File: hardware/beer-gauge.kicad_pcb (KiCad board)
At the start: 4 copper layers, 69.8 x 95.2 mm, 70 parts, among them J1 OLED_MODULE, P1 CONN_01X04, P2 CONN_01X04, P3 CONN_01X04, P4 CONN_01X04, P5 USB_OTG, SW1 SW_PUSH, U1 ADS1232, U2 LP38691, U3 MKL02Z32, U4 MK20DX256VLH7, U5 TCA9543A, U6 SN74LVC1G58, Y1 16 MHz, Y2 32.768 kHz

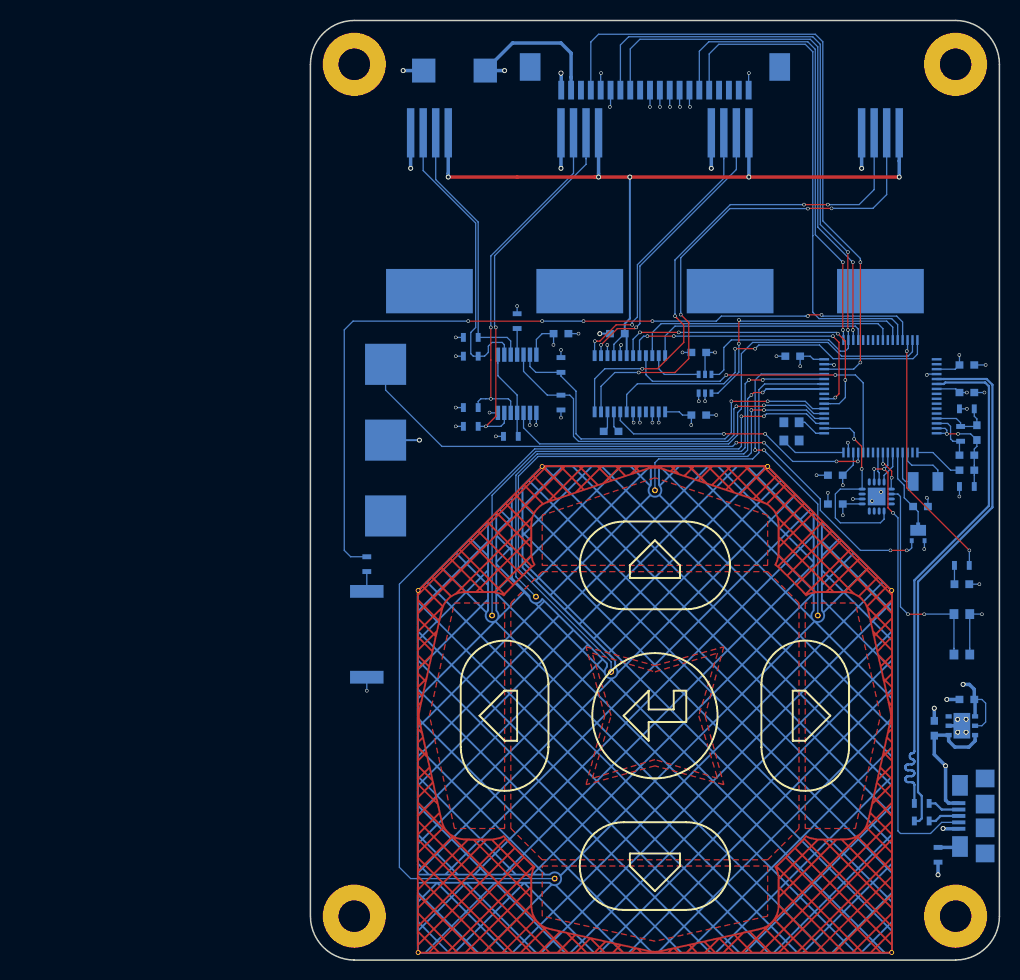
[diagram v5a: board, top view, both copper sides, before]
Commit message: Added DC jack for 5V input.  Updated layout
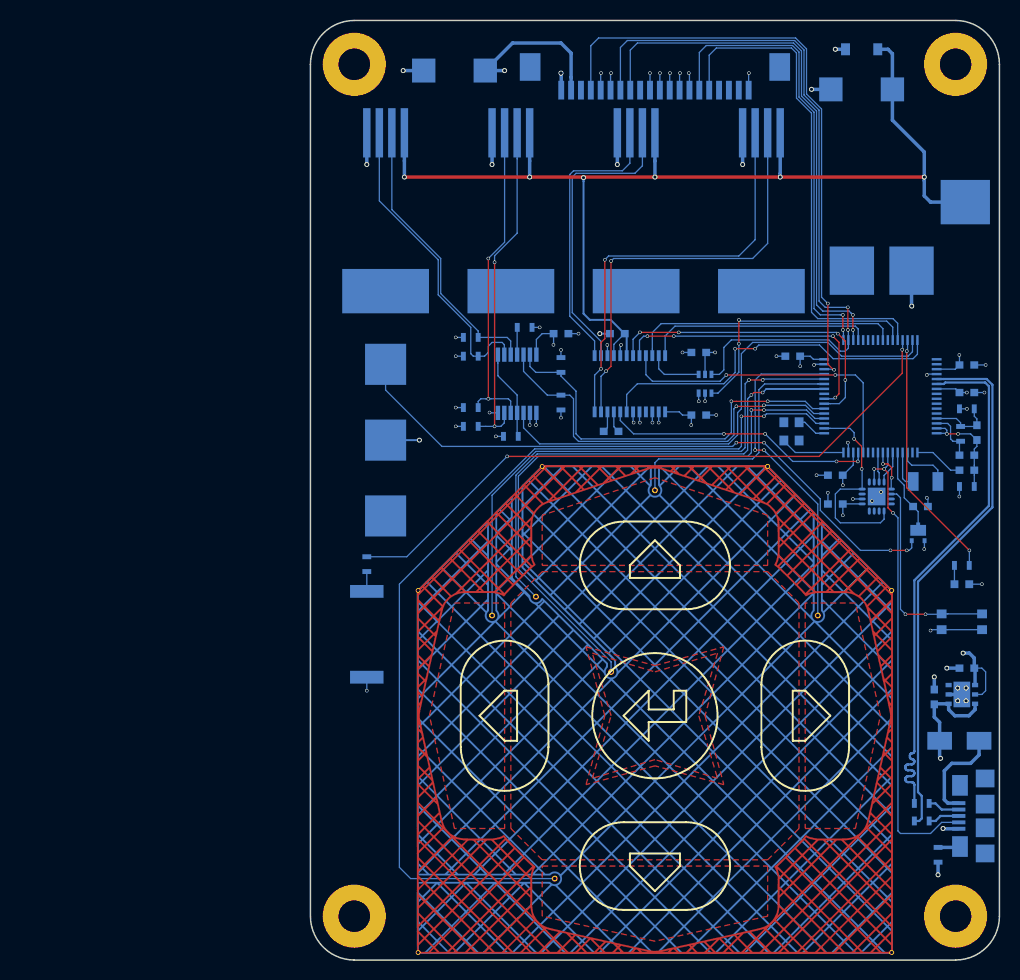
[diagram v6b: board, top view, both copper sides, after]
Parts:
- added C18: 100u, Capacitors_Tantalum_SMD:TantalC_SizeD_EIA-7343_Reflow, B.Cu at (193.0, 52.7)
- added CON1: BARREL_JACK, footprint:PJ-070AH-SMT, B.Cu at (196.8, 64.1)
- added D3: DDZ6V2B, Diodes_SMD:SOD-123, B.Cu at (193.0, 48.6)
- added D4: S1B, Diodes_SMD:SMA_Standard, B.Cu at (202.9, 118.7)
- moved P1 12.1 mm to (182.9, 64.8)
- moved P2 9.53 mm to (170.2, 64.8)
- moved P3 6.99 mm to (157.5, 64.8)
- moved P4 4.44 mm to (144.8, 64.8)
- moved C5 3.17 mm to (200.4, 114.3)
- moved C7 3.17 mm to (203.7, 111.4)
- moved U2 3.17 mm to (203.2, 114.0)
- moved SW1 1.27 mm to (203.2, 106.7), turned to 0 degrees
- moved R8 0.99 mm to (158.9, 76.8), turned to 180 degrees
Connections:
- P5 pad 1: +5V -> Net-(D4-Pad2)
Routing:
- net +5V: track 166.5 -> 192.2 mm, vias 6 -> 7
- net /Teensy/6: track 84.3 -> 65.4 mm, vias 6 -> 2
- net Net-(D4-Pad2): track 0.00 -> 10.2 mm
- net Net-(P1-Pad2): track 53.0 -> 43.5 mm, vias 4 -> 2
- net Net-(P1-Pad3): track 51.6 -> 42.8 mm, vias 4 -> 2
- net GND: track 78.8 -> 84.3 mm, vias 54 -> 57
- net /Teensy/9: track 67.1 -> 61.9 mm
- net Net-(P3-Pad2): track 37.9 -> 34.5 mm
- net Net-(P3-Pad3): track 35.8 -> 33.0 mm
- net Net-(P2-Pad3): track 31.4 -> 29.1 mm, vias 2 -> 0
- net Net-(P4-Pad2): track 27.4 -> 29.2 mm
- net Net-(P4-Pad3): track 30.4 -> 31.8 mm
- net /Teensy/8: track 52.0 -> 50.7 mm
- net Net-(SW1-Pad2): track 22.1 -> 20.9 mm
- net Net-(P2-Pad2): track 29.3 -> 30.2 mm, vias 2 -> 0
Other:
- board text added: "SCALE1"
- board text added: "SCALE2"
- board text added: "SENSOR1"
- board text added: "SENSOR2"
- board text removed: "SCALE 1"
- board text removed: "SCALE 2"
- board text removed: "SENSOR 1"
- board text removed: "SENSOR 2"
